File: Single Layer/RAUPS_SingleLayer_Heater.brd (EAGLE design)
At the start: 74 x 79.4 mm, 21 parts, among them Q1 STP55NF06L, Q2 STP55NF06L

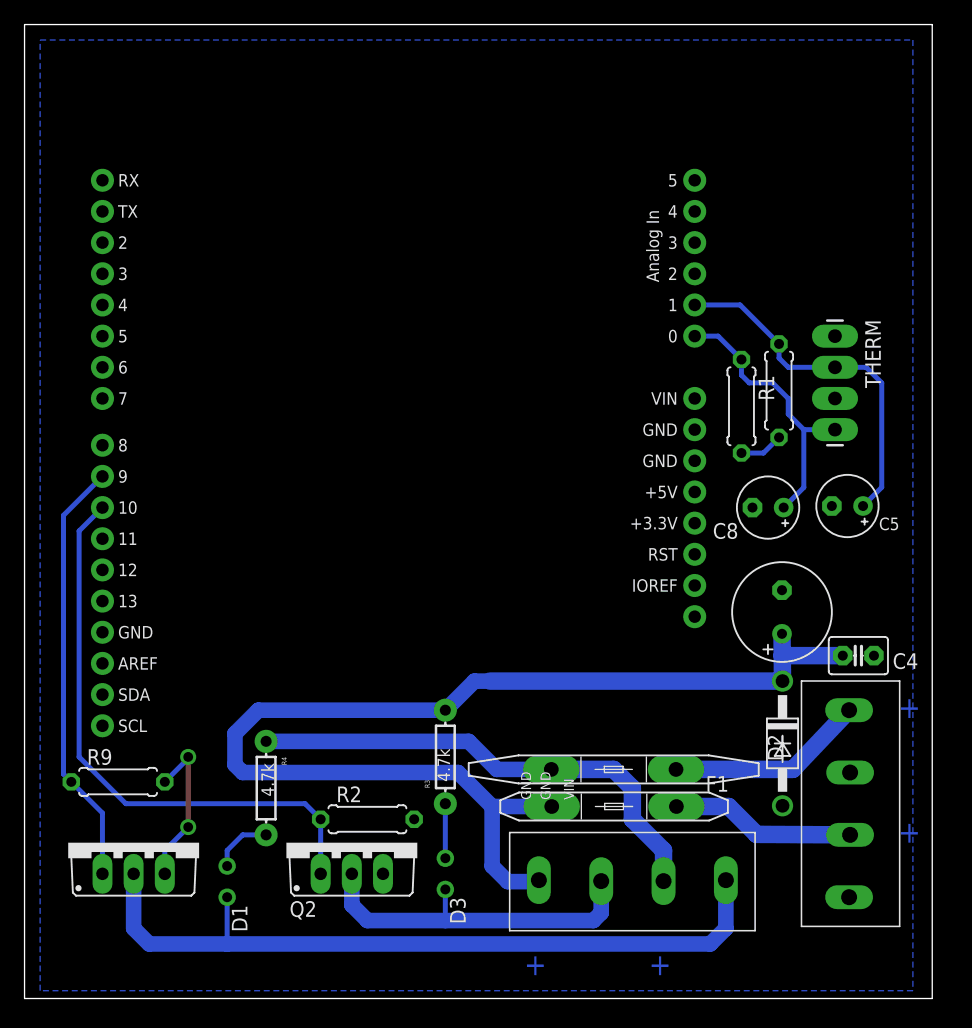
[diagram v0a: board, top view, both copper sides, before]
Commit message: Added BOM, final single layer board tweaks, and re-organized file structure to better reflect project goals
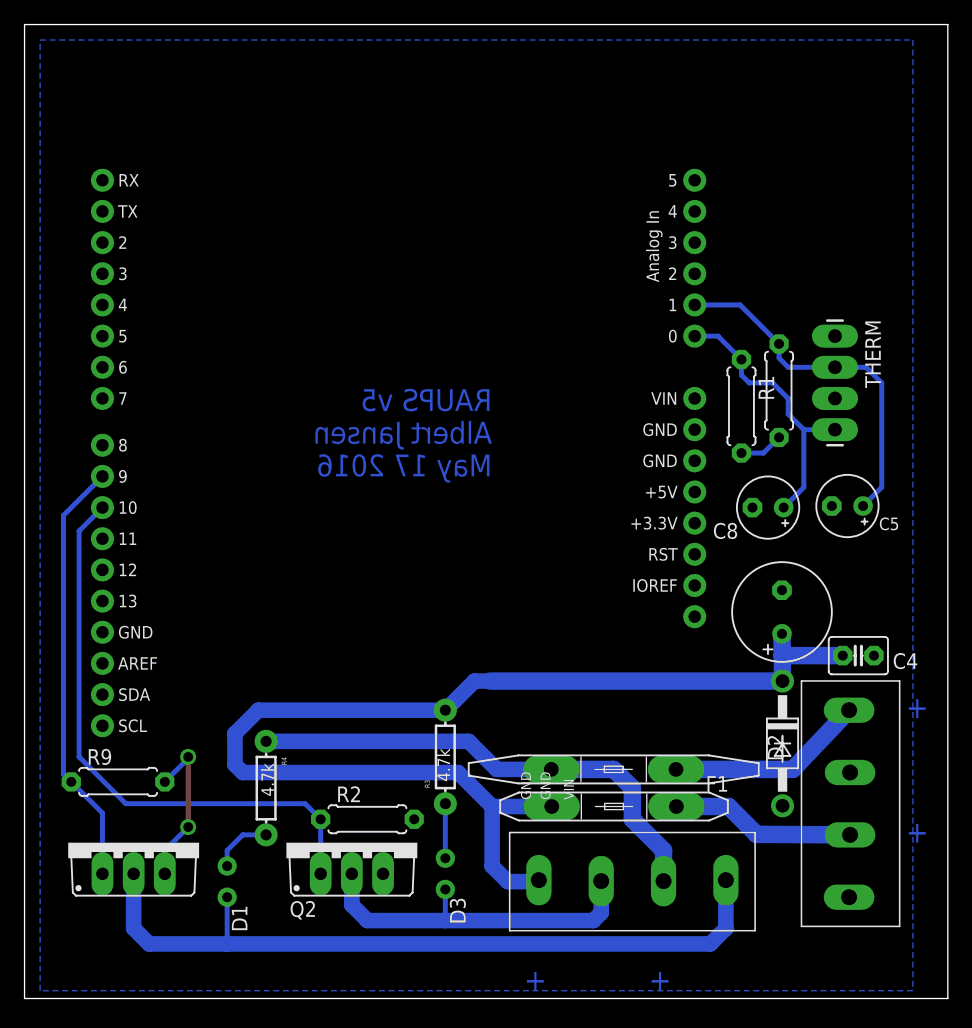
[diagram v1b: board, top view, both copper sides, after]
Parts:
- C6: value 470uF -> 100uF
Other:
- board size 74 x 79.4 mm -> 75.2 x 79.4 mm
- board text added: "RAUPS v5 Albert Jansen May 17 2016"
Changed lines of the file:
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@@
 <setting verticaltext="up"/>
 </settings>
-<grid distance="50" unitdist="mil" unit="mm" style="lines" multiple="1" display="no" altdistance="25" altunitdist="mil" altunit="mm"/>
+<grid distance="50" unitdist="mil" unit="mil" style="lines" multiple="1" display="no" altdistance="25" altunitdist="mil" altunit="mil"/>
 <layers>
 <layer number="1" name="Top" color="4" fill="1" visible="yes" active="yes"/>
@@
 <board>
 <plain>
-<wire x1="73.965" y1="3.175" x2="73.965" y2="82.54" width="0" layer="20"/>
-<wire x1="73.965" y1="82.54" x2="0" y2="82.54" width="0" layer="20"/>
+<wire x1="75.235" y1="3.175" x2="75.235" y2="82.54" width="0" layer="20"/>
+<wire x1="75.235" y1="82.54" x2="0" y2="82.54" width="0" layer="20"/>
 <wire x1="0" y1="82.54" x2="0" y2="3.175" width="0" layer="20"/>
-<wire x1="73.965" y1="3.175" x2="0" y2="3.175" width="0" layer="20"/>
+<wire x1="75.235" y1="3.175" x2="0" y2="3.175" width="0" layer="20"/>
 <text x="44.7675" y="19.3675" size="0.8128" layer="25" rot="R90">VIN</text>
 <text x="42.8625" y="19.3675" size="0.8128" layer="25" rot="R90">GND</text>
 <text x="41.275" y="19.3675" size="0.8128" layer="25" rot="R90">GND</text>
-<text x="73.025" y="26.035" size="1.778" layer="16" rot="MR0">+</text>
-<text x="73.025" y="15.875" size="1.778" layer="16" rot="MR0">+</text>
-<text x="42.545" y="5.08" size="1.778" layer="16" rot="MR0">+</text>
-<text x="52.705" y="5.08" size="1.778" layer="16" rot="MR0">+</text>
+<text x="73.66" y="26.035" size="1.778" layer="16" rot="MR0">+</text>
+<text x="73.66" y="15.875" size="1.778" layer="16" rot="MR0">+</text>
+<text x="42.545" y="3.81" size="1.778" layer="16" rot="MR0">+</text>
+<text x="52.705" y="3.81" size="1.778" layer="16" rot="MR0">+</text>
+<text x="38.1" y="45.72" size="1.778" layer="16" font="vector" rot="MR0">RAUPS v5
+Albert Jansen
+May 17 2016</text>
+<polygon width="0.4064" layer="42">
+<vertex x="17.78" y="54.61"/>
+<vertex x="40.64" y="54.61"/>
+<vertex x="40.64" y="44.45"/>
+<vertex x="40.64" y="43.18"/>
+<vertex x="16.51" y="43.18"/>
+<vertex x="16.51" y="54.61"/>
+</polygon>
 </plain>
 <attributes>
@@
 </class>
 </classes>
-<designrules name="Humber Safe DRU">
+<designrules name="Humber Safe DRU *">
 <description language="en">&lt;b&gt;EAGLE Design Rules&lt;/b&gt;
 &lt;p&gt;
@@
 <param name="rvMicroViaOuter" value="0.25"/>
 <param name="rvMicroViaInner" value="0.25"/>
-<param name="rlMinPadTop" value="12mil"/>
+<param name="rlMinPadTop" value="15mil"/>
 <param name="rlMaxPadTop" value="20mil"/>
 <param name="rlMinPadInner" value="10mil"/>
 <param name="rlMaxPadInner" value="20mil"/>
-<param name="rlMinPadBottom" value="12mil"/>
+<param name="rlMinPadBottom" value="15mil"/>
 <param name="rlMaxPadBottom" value="20mil"/>
 <param name="rlMinViaOuter" value="10mil"/>
@@
 <attribute name="VALUE" x="72.9615" y="29.6545" size="0.8128" layer="27" ratio="10"/>
 </element>
-<element name="C6" library="adafruit" package="E3,5-8" value="470uF" x="61.722" y="34.671" smashed="yes" rot="R90"/>
+<element name="C6" library="adafruit" package="E3,5-8" value="100uF" x="61.722" y="34.671" smashed="yes" rot="R90"/>
 <element name="F1" library="RepRapjr" package="MFR500" value="MFR500" x="48.0388375" y="18.8208125" smashed="yes">
 <attribute name="NAME" x="55.5001375" y="20.0273125" size="1.27" layer="25" ratio="10"/>
@@
 <contactref element="U$1" pad="P4"/>
 <contactref element="D2" pad="A"/>
-<polygon width="0.4064" layer="16">
+<polygon width="0.4064" layer="16" isolate="0.6096">
 <vertex x="1.27" y="81.28"/>
 <vertex x="72.39" y="81.28"/>
@@
 </board>
 </drawing>
+<compatibility>
+<note version="6.3" minversion="6.2.2" severity="warning">
+Since Version 6.2.2 text objects can contain more than one line,
+which will not be processed correctly with this version.
+</note>
+</compatibility>
 </eagle>
